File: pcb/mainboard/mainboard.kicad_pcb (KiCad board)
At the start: 10 copper layers, 165 x 121 mm, 608 parts, among them J1 CONN_PCIE_PWR_8PIN, J10 FAN_01, J11 XILINX_JTAG, J12 JUMPER_0402_SPDT, J13 JUMPER_0402_SPDT, J14 RJ45, J15 PMOD_HOST, J16 SMPM, J17 SMPM, J18 SMPM, J19 SMPM, J2 CONN_IBC_MGMT, J20 SMPM, J21 SMPM, J22 SMPM, J23 SMPM, J24 SMPM, J25 SMPM, J26 SMPM, J27 0826-1G1T-23-F, J28 SMPM, J29 SMPM, J3 CONN_01X03, J30 SMPM, J31 SMPM, J32 SMPM, J33 SMPM, J34 SMPM, J35 SMPM, J36 SMPM, J37 SMPM, J38 SMPM, J39 SMPM, J4 CONN_01X05, J40 SMPM, J41 SMPM, J42 SMPM, J43 SMPM, J44 SMPM, J45 SMPM, J46 SMPM, J47 SMPM, J48 CONN_01X10, J5 XILINX_JTAG, J6 CONN_SFP_HOST, J7 SFP_CAGE, J8 FAN_01, J9 CONN_01X03, K1 RELAY_TE_HF3_96, K2 RELAY_TE_HF3_96, K3 RELAY_TE_HF3_96, K4 RELAY_TE_HF3_96, M1 960-23-23-F-AB-0, SW1 SWITCH, SW2 SWITCH, U1 STM32L031C6U6, U10 MAX40026, U11 MAX40026, U12 MAX40026, U13 MAX40026, U14 MAX40026, U15 MAX40026, U16 MAX40026, U17 MAX40026, U18 MAX40026, U19 MAX40026, U2 MYMGK1R812ERSR, U20 MAX40026, U21 DAC60508, U22 DAC60508, U23 STM32H735-UFBGA176-25, U24 AT24MAC402, U25 ADM3101E_QFN, U26 LMR70503, U27 SIT9121AI-2BF-XXS200.000000G, U28 SIT9121AI-2BF-XXS156.250000G, U29 HMC675LP3E, U3 MYMGK00504ERSR, U30 SIT9121AI-2BF-XXS200.000000G, U31 ECS-1612MV-250-CN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

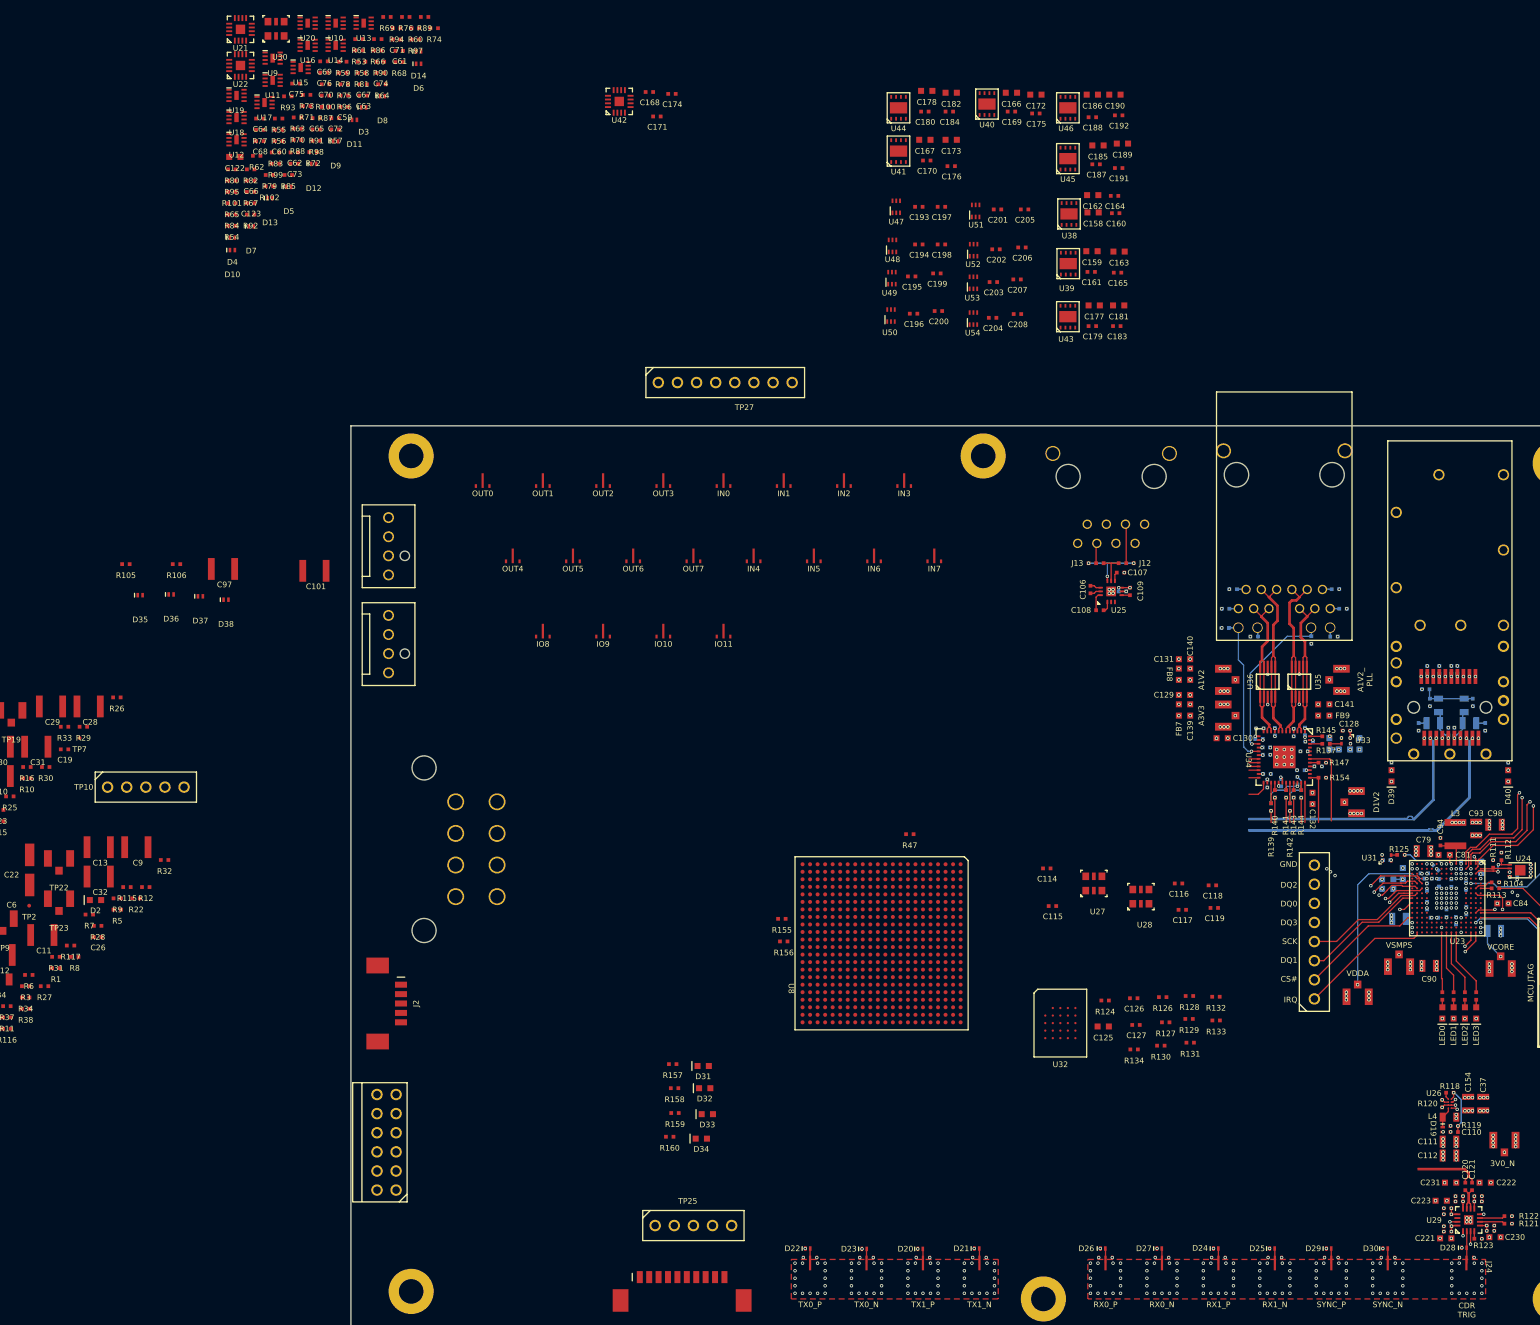
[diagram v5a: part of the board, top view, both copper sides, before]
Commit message: Started layout of rear panel IO connectors and associated drivers/comparators
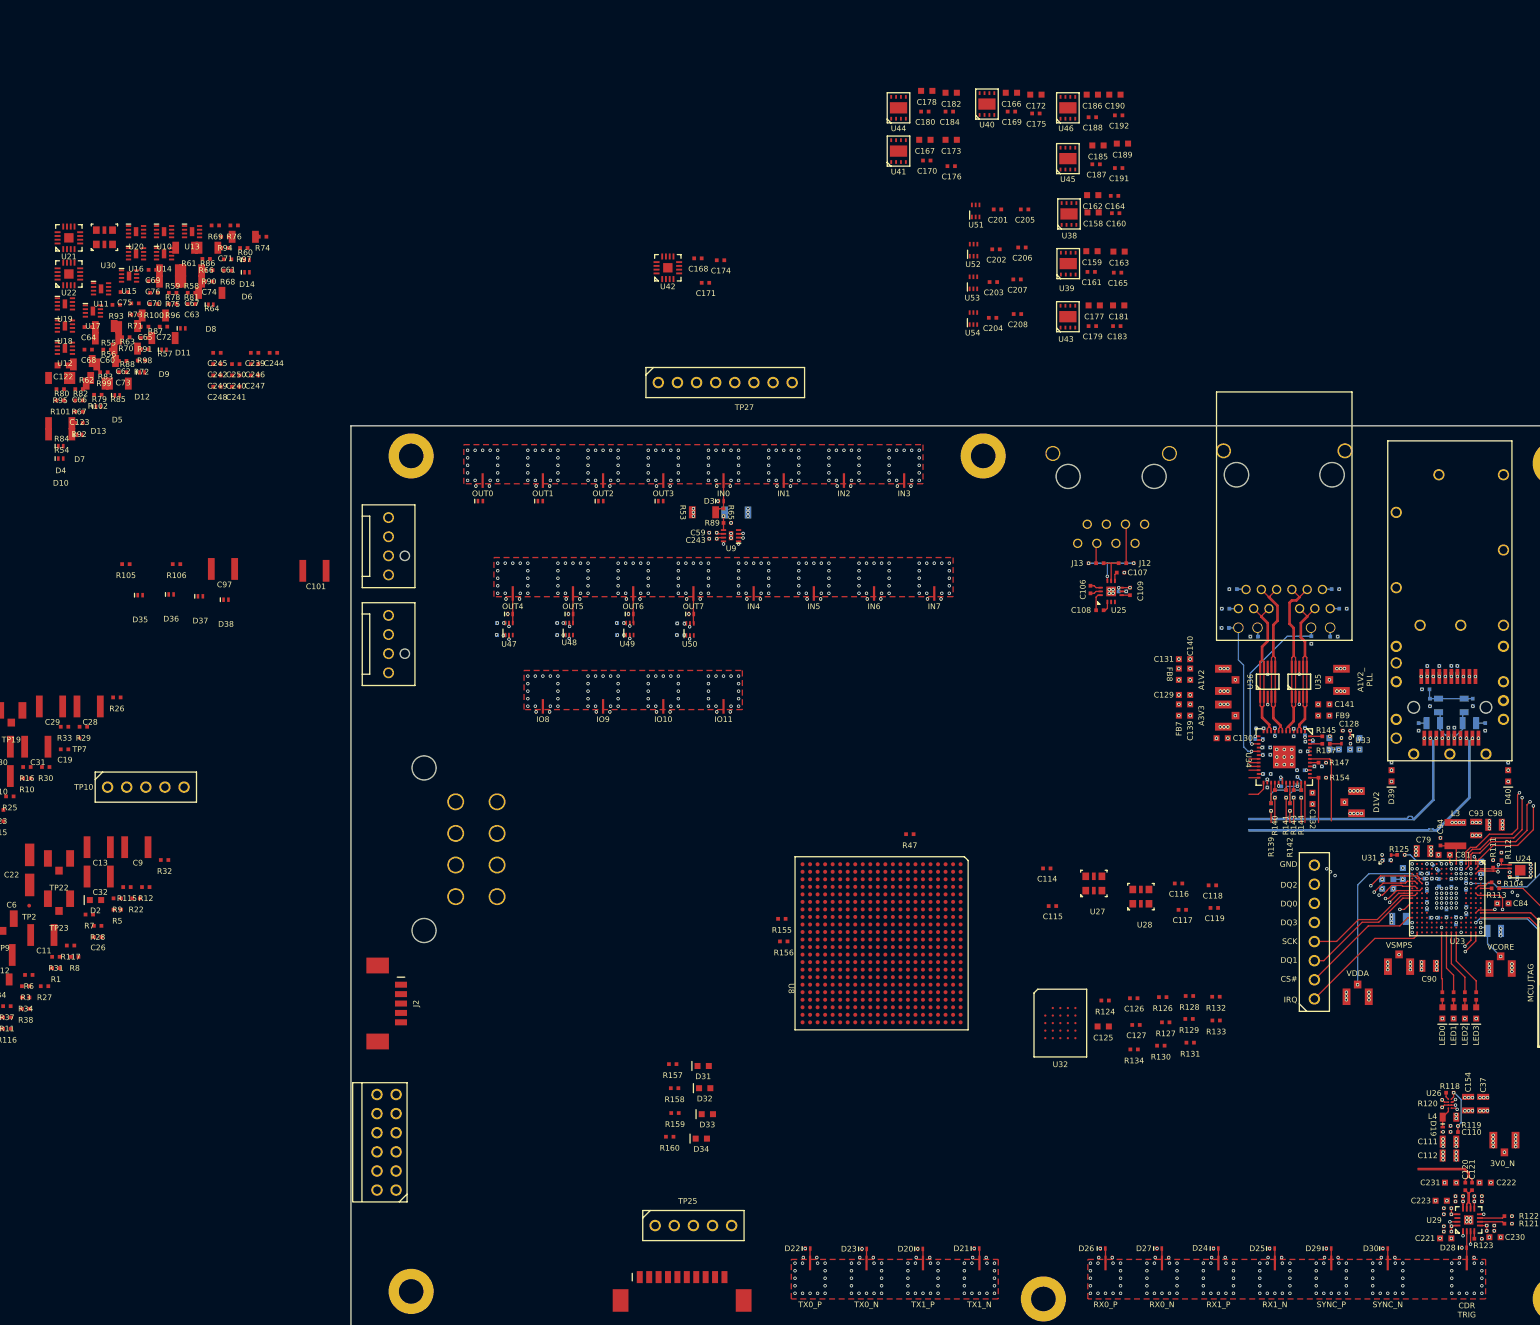
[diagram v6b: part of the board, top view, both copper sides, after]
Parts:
- added C239: 0.47 uF, azonenberg_pcb:EIA_0402_CAP_NOSILK, F.Cu at (102.2, 10.3)
- added C240: 0.47 uF, azonenberg_pcb:EIA_0402_CAP_NOSILK, F.Cu at (99.7, 13.3)
- added C241: 0.47 uF, azonenberg_pcb:EIA_0402_CAP_NOSILK, F.Cu at (99.7, 14.8)
- added C242: 0.47 uF, azonenberg_pcb:EIA_0402_CAP_NOSILK, F.Cu at (97.2, 11.8)
- added C243: 0.47 uF, azonenberg_pcb:EIA_0402_CAP_NOSILK, F.Cu at (163.1, 35.0)
- added C244: 0.47 uF, azonenberg_pcb:EIA_0402_CAP_NOSILK, F.Cu at (104.7, 10.3)
- added C245: 0.47 uF, azonenberg_pcb:EIA_0402_CAP_NOSILK, F.Cu at (97.2, 10.3)
- added C246: 0.47 uF, azonenberg_pcb:EIA_0402_CAP_NOSILK, F.Cu at (102.2, 11.8)
- added C247: 0.47 uF, azonenberg_pcb:EIA_0402_CAP_NOSILK, F.Cu at (102.2, 13.3)
- added C248: 0.47 uF, azonenberg_pcb:EIA_0402_CAP_NOSILK, F.Cu at (97.2, 14.8)
- added C249: 0.47 uF, azonenberg_pcb:EIA_0402_CAP_NOSILK, F.Cu at (97.2, 13.3)
- added C250: 0.47 uF, azonenberg_pcb:EIA_0402_CAP_NOSILK, F.Cu at (99.7, 11.8)
- added D41: SZESD7471N2T5G, azonenberg_pcb:SOD882, F.Cu at (132.2, 30.0)
- added D42: SZESD7471N2T5G, azonenberg_pcb:SOD882, F.Cu at (156.2, 30.0)
- added D43: SZESD7471N2T5G, azonenberg_pcb:SOD882, F.Cu at (152.2, 45.0)
- added D44: SZESD7471N2T5G, azonenberg_pcb:SOD882, F.Cu at (140.2, 30.0)
- added D45: SZESD7471N2T5G, azonenberg_pcb:SOD882, F.Cu at (136.2, 45.0)
- added D46: SZESD7471N2T5G, azonenberg_pcb:SOD882, F.Cu at (160.2, 45.0)
- added D47: SZESD7471N2T5G, azonenberg_pcb:SOD882, F.Cu at (148.2, 30.0)
- added D48: SZESD7471N2T5G, azonenberg_pcb:SOD882, F.Cu at (144.2, 45.0)
- C193, C194, C195, C196, C197, C198, C199, C200: moved to B.Cu
- R53, R54, R55, R56, R57, R58, R59, R60, R61, R62, R63, R64, R78, R79, R80, R81, R82, R83, R84, R85, R86, R87, R88: footprint azonenberg_pcb:EIA_0402_RES_NOSILK -> azonenberg_pcb:EIA_1206_CAP_NOSILK
- R77: footprint azonenberg_pcb:EIA_0402_RES_NOSILK -> azonenberg_pcb:EIA_1206_CAP_NOSILK; moved to B.Cu
- moved U9 87.9 mm to (165.5, 34.6), turned to 180 degrees
- moved C197 81.6 mm to (134.9, 47.8), turned to 180 degrees
- moved R77 81.2 mm to (166.2, 31.5), turned to 180 degrees
- moved C193 78.4 mm to (134.9, 46.2), turned to 180 degrees
- moved R89 78.3 mm to (165.0, 32.9)
- moved R65 77.2 mm to (164.5, 31.5), turned to -90 degrees
- moved R53 76.6 mm to (161.9, 31.5), turned to 180 degrees
- moved U47 76.1 mm to (136.0, 47.0)
- moved C59 74.8 mm to (163.1, 34.2), turned to 180 degrees
- moved C198 72.4 mm to (142.9, 47.8), turned to 180 degrees
- moved D3 70.7 mm to (164.2, 30.0)
- moved C194 69.2 mm to (142.9, 46.2), turned to 180 degrees
- moved U48 66.6 mm to (144.0, 47.0)
- moved C199 63.8 mm to (150.8, 47.8), turned to 180 degrees
- moved C195 60.1 mm to (150.8, 46.2), turned to 180 degrees
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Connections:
- J24 pad 1: (no net) -> /Transceivers/CDRTRIG_IN
- J24 pad 2: (no net) -> /GND
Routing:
- net /GND: track 754.8 -> 1074.5 mm, vias 426 -> 796
- net /3V3: track 290.5 -> 324.5 mm, vias 65 -> 75
- net /Connectors/IN0: track 0.00 -> 4.98 mm
- net /Connectors/OUT7: track 0.00 -> 4.00 mm
- net /Connectors/OUT6: track 0.00 -> 3.95 mm
- net /Connectors/OUT5: track 0.00 -> 3.93 mm
- net /Connectors/OUT4: track 0.00 -> 3.93 mm
- net /Inputs/VFE_IN0: track 0.00 -> 1.85 mm, vias 0 -> 1
- net /Inputs/TRIGIN_0_P: track 0.00 -> 0.35 mm, vias 0 -> 1
- net /Inputs/TRIGIN_0_N: track 0.00 -> 0.35 mm, vias 0 -> 1
- net /Output/VCCIO_5: track 0.00 -> 0.20 mm, vias 0 -> 1
- net /Output/VCCIO_6: track 0.00 -> 0.10 mm, vias 0 -> 1
- net /Output/VCCIO_4: track 0.00 -> 0.10 mm, vias 0 -> 1
- net /Output/VCCIO_7: track 0.00 -> 0.07 mm, vias 0 -> 1

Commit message: Grouped remaining components by subsystem, continued layout of IO area
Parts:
- C160, C164, R78, R79, R80: moved to B.Cu
- moved U3 224.9 mm to (236.8, 150.3)
- moved TP1 213.1 mm to (242.8, 146.8)
- moved TP19 212.1 mm to (261.5, 148.8)
- moved R29 209.3 mm to (268.8, 149.2)
- moved FB2 200.9 mm to (255.0, 147.0)
- moved C2 194.3 mm to (228.0, 147.0)
- moved C12 189.6 mm to (249.2, 147.2)
- moved C5 189.2 mm to (227.0, 152.8)
- moved R28 187.5 mm to (257.2, 151.5)
- moved R12 180.6 mm to (254.2, 151.2)
- moved R9 179.2 mm to (249.2, 152.0)
- moved C9 173.8 mm to (243.2, 151.0)
- moved R3 159.2 mm to (221.2, 149.2)
- moved R1 155.1 mm to (221.2, 146.0)
- moved R35 143.9 mm to (176.2, 153.5)
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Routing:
- net /GND: track 1074.5 -> 1158.0 mm, vias 796 -> 838
- net /VREF_SERDESIN: track 8.70 -> 69.6 mm, vias 1 -> 2
- net /Transceivers/FASTSYNC_TX_N: track 1.92 -> 60.3 mm, vias 0 -> 1
- net /Transceivers/CDRTRIG_RX_P: track 8.23 -> 61.7 mm, vias 0 -> 2
- net /Transceivers/CDRTRIG_RX_N: track 8.53 -> 61.7 mm, vias 0 -> 2
- net /3V3: track 324.5 -> 376.7 mm, vias 75 -> 81
- net /Transceivers/FASTSYNC_TX_P: track 1.93 -> 53.7 mm, vias 0 -> 1
- net /Transceivers/BERT_RX1_N: track 1.95 -> 47.1 mm, vias 0 -> 1
- net /Power Supply/3V0_N_EN: track 5.37 -> 47.4 mm, vias 1 -> 2
- net /Transceivers/BERT_RX1_P: track 1.95 -> 41.1 mm, vias 0 -> 1
- net /Transceivers/BERT_RX0_N: track 1.95 -> 35.5 mm, vias 0 -> 1
- net /Transceivers/BERT_RX0_P: track 1.95 -> 30.8 mm, vias 0 -> 1
- net /Output/VCCIO_4: track 0.10 -> 10.5 mm, vias 1 -> 4
- net /Connectors/IN3: track 0.00 -> 5.12 mm
- net /Connectors/IN1: track 0.00 -> 5.08 mm
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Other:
- board text added: "12V input"
- board text added: "1V0 supply"
- board text added: "1V2 supply"
- board text added: "1V8 supply"
- board text added: "3V3 supply"
- board text added: "5V0 supply"
- board text added: "GTX_1V0 supply"
- board text added: "GTX_1V8 supply"
- board text added: "Management"
- board text added: "Power switches"

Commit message: Initial FPGA routing
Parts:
- added R165: 4.7K, azonenberg_pcb:EIA_0402_RES_NOSILK, B.Cu at (253.0, 104.8)
- C125, C126, C127, C177, C181, C201, C203, C205, C207, C209, C210, C211, C212, R1, R101, R124, R126, R127, R128, R129, R3, R81, R82, R83, R84, R85, R87, U55, U56: moved to B.Cu
- C160, C164: moved to F.Cu
- moved C18 221.5 mm to (235.9, 149.3)
- moved C30 221.5 mm to (245.5, 149.5)
- moved C33 221.5 mm to (245.1, 155.9)
- moved R19 221.5 mm to (241.1, 148.9)
- moved R37 221.5 mm to (254.5, 155.5)
- moved TP7 221.5 mm to (240.5, 154.9)
- moved C24 221.5 mm to (235.7, 155.1)
- moved FB5 221.5 mm to (250.7, 153.5)
- moved R22 221.5 mm to (240.7, 151.7)
- moved R25 221.5 mm to (249.7, 148.7)
- moved R33 221.5 mm to (258.9, 155.9)
- moved TP23 221.5 mm to (255.7, 149.5)
- moved U7 221.5 mm to (226.0, 153.0)
- moved K3 143.8 mm to (156.5, 66.5), turned to 180 degrees
- moved TP28 142.9 mm to (130.0, 62.5), turned to 90 degrees
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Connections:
- D11 pad 2: /Connectors/IN8 -> /Connectors/IO8
- D12 pad 2: /Connectors/IN9 -> /Connectors/IO11
- D13 pad 2: /Connectors/IN10 -> /Connectors/IO9
- D14 pad 2: /Connectors/IN11 -> /Connectors/IO10
- U21 pad 10: /Inputs/VREF_IN6 -> /Inputs/VREF_IN1
- U21 pad 11: /Inputs/VREF_IN7 -> /Inputs/VREF_IN0
- U21 pad 2: /Inputs/VREF_IN0 -> /Inputs/VREF_IN3
- U21 pad 3: /Inputs/VREF_IN1 -> /Inputs/VREF_IN2
- U21 pad 4: /Inputs/VREF_IN2 -> /Inputs/VREF_IN7
- U21 pad 5: /Inputs/VREF_IN3 -> /Inputs/VREF_IN6
- U21 pad 8: /Inputs/VREF_IN4 -> /Inputs/VREF_IN5
- U21 pad 9: /Inputs/VREF_IN5 -> /Inputs/VREF_IN4
- U8 pad A10: unconnected-(U8-PadA10) -> /1000base-T PHY/RGMII_TX_EN
- U8 pad A11: unconnected-(U8-PadA11) -> /1000base-T PHY/ETH_RXD2
- U8 pad A13: /Output/OUT10_3V3 -> unconnected-(U8-PadA13)
- U8 pad A14: /Output/OUT11_3V3 -> unconnected-(U8-PadA14)
- U8 pad A16: /Connectors/OE11B -> unconnected-(U8-PadA16)
- U8 pad A8: unconnected-(U8-PadA8) -> /1000base-T PHY/RGMII_TXD1
- U8 pad A9: unconnected-(U8-PadA9) -> /1000base-T PHY/RGMII_TXD3
- U8 pad AA10: unconnected-(U8-PadAA10) -> /Inputs/TRIGIN_3_P
- U8 pad AA17: /1V8 -> /3V3
- U8 pad AA20: unconnected-(U8-PadAA20) -> /Connectors/OE10B
- U8 pad AA3: unconnected-(U8-PadAA3) -> /Connectors/OUT0
- U8 pad AA4: unconnected-(U8-PadAA4) -> /Connectors/OUT2
- U8 pad AA5: unconnected-(U8-PadAA5) -> /Inputs/TRIGIN_0_P
- U8 pad AA6: unconnected-(U8-PadAA6) -> /Inputs/TRIGIN_2_P
- U8 pad AA8: unconnected-(U8-PadAA8) -> /Inputs/TRIGIN_4_N
- U8 pad AA9: unconnected-(U8-PadAA9) -> /Inputs/TRIGIN_4_P
- U8 pad AB10: unconnected-(U8-PadAB10) -> /Inputs/TRIGIN_3_N
- U8 pad AB14: /1V8 -> /3V3
- U8 pad AB2: unconnected-(U8-PadAB2) -> /Connectors/OUT1
- U8 pad AB21: unconnected-(U8-PadAB21) -> /Connectors/OE11B
- U8 pad AB3: unconnected-(U8-PadAB3) -> /Connectors/OUT3
- U8 pad AB5: unconnected-(U8-PadAB5) -> /Inputs/TRIGIN_0_N
- U8 pad AB6: unconnected-(U8-PadAB6) -> /Inputs/TRIGIN_2_N
- U8 pad AB7: unconnected-(U8-PadAB7) -> /Inputs/TRIGIN_1_N
- U8 pad AB8: unconnected-(U8-PadAB8) -> /Inputs/TRIGIN_1_P
- U8 pad B10: unconnected-(U8-PadB10) -> /1000base-T PHY/RGMII_TX_CLK
- U8 pad B11: unconnected-(U8-PadB11) -> /1000base-T PHY/ETH_RXD3
- U8 pad B12: /Output/OUT7_3V3 -> unconnected-(U8-PadB12)
- U8 pad B13: /Connectors/OE9A -> unconnected-(U8-PadB13)
- U8 pad B16: /Connectors/OE10B -> unconnected-(U8-PadB16)
- U8 pad B8: unconnected-(U8-PadB8) -> /1000base-T PHY/RGMII_TXD0
- U8 pad C10: /1000base-T PHY/RGMII_TXD3 -> unconnected-(U8-PadC10)
- U8 pad C12: /Output/OUT6_3V3 -> unconnected-(U8-PadC12)
- U8 pad C13: /Connectors/OE8A -> unconnected-(U8-PadC13)
- U8 pad C14: /Connectors/OE8B -> unconnected-(U8-PadC14)
- U8 pad C15: /Connectors/OE9B -> unconnected-(U8-PadC15)
- U8 pad C9: unconnected-(U8-PadC9) -> /1000base-T PHY/RGMII_TXD2
- U8 pad D10: /1000base-T PHY/RGMII_TX_CLK -> unconnected-(U8-PadD10)
- U8 pad D11: /1000base-T PHY/ETH_MDC -> /1000base-T PHY/ETH_RXD1
- U8 pad D14: /Connectors/OE11A -> unconnected-(U8-PadD14)
- U8 pad E14: /Connectors/OE10A -> unconnected-(U8-PadE14)
- U8 pad E9: /1000base-T PHY/ETH_RXD3 -> unconnected-(U8-PadE9)
- U8 pad F1: /Transceivers/SFP_TX_N -> /Transceivers/SFP_TX_P
- U8 pad F13: /1000base-T PHY/RGMII_TXD1 -> unconnected-(U8-PadF13)
- U8 pad F14: /1000base-T PHY/RGMII_TX_EN -> unconnected-(U8-PadF14)
- U8 pad F15: /Output/OUT8_3V3 -> unconnected-(U8-PadF15)
- U8 pad F16: /Output/OUT9_3V3 -> unconnected-(U8-PadF16)
- U8 pad F2: /Transceivers/SFP_TX_P -> /Transceivers/SFP_TX_N
- U8 pad F9: /1000base-T PHY/ETH_RXD2 -> unconnected-(U8-PadF9)
- U8 pad G12: /1000base-T PHY/ETH_RXD1 -> /1000base-T PHY/ETH_MDC
- U8 pad G13: /1000base-T PHY/RGMII_TXD2 -> unconnected-(U8-PadG13)
- U8 pad G15: /Output/OUT4_3V3 -> unconnected-(U8-PadG15)
- U8 pad G16: /Output/OUT5_3V3 -> unconnected-(U8-PadG16)
- U8 pad H14: /1000base-T PHY/RGMII_TXD0 -> unconnected-(U8-PadH14)
- U8 pad K1: /Inputs/TRIGIN_1_P -> unconnected-(U8-PadK1)
- U8 pad K2: /Inputs/TRIGIN_3_N -> unconnected-(U8-PadK2)
- U8 pad K3: /Inputs/TRIGIN_3_P -> unconnected-(U8-PadK3)
- U8 pad K4: Net-(R101-Pad2) -> Net-(R155-Pad2)
- U8 pad L1: /Inputs/TRIGIN_1_N -> unconnected-(U8-PadL1)
- U8 pad L3: /Inputs/TRIGIN_0_P -> unconnected-(U8-PadL3)
- U8 pad L4: /Inputs/TRIGIN_5_N -> unconnected-(U8-PadL4)
- U8 pad L5: /Inputs/TRIGIN_5_P -> unconnected-(U8-PadL5)
- U8 pad M1: /Inputs/TRIGIN_2_N -> unconnected-(U8-PadM1)
- U8 pad M2: /Inputs/TRIGIN_2_P -> unconnected-(U8-PadM2)
- U8 pad M3: /Inputs/TRIGIN_0_N -> unconnected-(U8-PadM3)
- U8 pad M5: /Inputs/TRIGIN_8_P -> unconnected-(U8-PadM5)
- U8 pad N2: /Inputs/TRIGIN_4_N -> unconnected-(U8-PadN2)
- U8 pad N3: /Inputs/TRIGIN_4_P -> unconnected-(U8-PadN3)
- U8 pad N4: /Inputs/TRIGIN_8_N -> unconnected-(U8-PadN4)
- U8 pad P1: /Inputs/TRIGIN_7_P -> unconnected-(U8-PadP1)
- U8 pad P2: /Inputs/TRIGIN_6_P -> unconnected-(U8-PadP2)
- U8 pad R1: /Inputs/TRIGIN_7_N -> unconnected-(U8-PadR1)
- U8 pad R2: /Inputs/TRIGIN_6_N -> unconnected-(U8-PadR2)
- U8 pad R3: /Inputs/CLK_200_P -> unconnected-(U8-PadR3)
- U8 pad R6: unconnected-(U8-PadR6) -> /Inputs/TRIGIN_7_N
- U8 pad R7: unconnected-(U8-PadR7) -> /Inputs/TRIGIN_7_P
- U8 pad T1: /Inputs/TRIGIN_9_P -> unconnected-(U8-PadT1)
- U8 pad T10: unconnected-(U8-PadT10) -> /Inputs/TRIGIN_11_N
- U8 pad T11: unconnected-(U8-PadT11) -> /Inputs/TRIGIN_11_P
- U8 pad T13: /Connectors/OUT2 -> unconnected-(U8-PadT13)
- U8 pad T14: Net-(R156-Pad2) -> Net-(R102-Pad2)
- U8 pad T18: unconnected-(U8-PadT18) -> /Output/OUT8_3V3
- U8 pad T20: unconnected-(U8-PadT20) -> /Connectors/OE10A
- U8 pad T21: unconnected-(U8-PadT21) -> /Output/OUT4_3V3
- U8 pad T22: /1V8 -> /3V3
- U8 pad T3: /Inputs/CLK_200_N -> unconnected-(U8-PadT3)
- U8 pad T5: /Inputs/TRIGIN_11_P -> unconnected-(U8-PadT5)
- U8 pad T6: Net-(R155-Pad2) -> Net-(R101-Pad2)
- U8 pad U1: /Inputs/TRIGIN_9_N -> unconnected-(U8-PadU1)
- U8 pad U13: /Connectors/OUT3 -> unconnected-(U8-PadU13)
- U8 pad U17: unconnected-(U8-PadU17) -> /Connectors/OE8A
- U8 pad U18: unconnected-(U8-PadU18) -> /Output/OUT9_3V3
- U8 pad U19: /1V8 -> /3V3
- U8 pad U2: /Inputs/TRIGIN_10_P -> unconnected-(U8-PadU2)
- U8 pad U20: unconnected-(U8-PadU20) -> /Connectors/OE11A
- U8 pad U21: unconnected-(U8-PadU21) -> /Output/OUT5_3V3
- U8 pad U22: unconnected-(U8-PadU22) -> /Output/OUT6_3V3
- U8 pad U5: /Inputs/TRIGIN_11_N -> unconnected-(U8-PadU5)
- U8 pad U6: unconnected-(U8-PadU6) -> /Inputs/TRIGIN_9_N
- U8 pad U7: unconnected-(U8-PadU7) -> /Inputs/TRIGIN_9_P
- U8 pad U8: unconnected-(U8-PadU8) -> /Inputs/TRIGIN_8_P
- U8 pad V10: unconnected-(U8-PadV10) -> /Inputs/TRIGIN_10_P
- U8 pad V12: /Connectors/OUT1 -> unconnected-(U8-PadV12)
- U8 pad V13: /Connectors/OUT0 -> unconnected-(U8-PadV13)
- U8 pad V16: /1V8 -> /3V3
- U8 pad V18: unconnected-(U8-PadV18) -> /Connectors/OE9A
- U8 pad V2: /Inputs/TRIGIN_10_N -> unconnected-(U8-PadV2)
- U8 pad V22: unconnected-(U8-PadV22) -> /Output/OUT7_3V3
- U8 pad V5: Net-(R102-Pad2) -> Net-(R156-Pad2)
- U8 pad V8: unconnected-(U8-PadV8) -> /Inputs/TRIGIN_8_N
- U8 pad W10: unconnected-(U8-PadW10) -> /Inputs/TRIGIN_10_N
- U8 pad W11: unconnected-(U8-PadW11) -> /Inputs/TRIGIN_5_P
- U8 pad W21: unconnected-(U8-PadW21) -> /Output/OUT10_3V3
- U8 pad W22: unconnected-(U8-PadW22) -> /Output/OUT11_3V3
- U8 pad W6: unconnected-(U8-PadW6) -> /Inputs/TRIGIN_6_P
- U8 pad Y11: unconnected-(U8-PadY11) -> /Inputs/TRIGIN_5_N
- U8 pad Y20: /1V8 -> /3V3
- U8 pad Y21: unconnected-(U8-PadY21) -> /Connectors/OE8B
- U8 pad Y22: unconnected-(U8-PadY22) -> /Connectors/OE9B
- U8 pad Y6: unconnected-(U8-PadY6) -> /Inputs/TRIGIN_6_N
- U8 pad Y7: unconnected-(U8-PadY7) -> /Inputs/CLK_200_N
- U8 pad Y8: unconnected-(U8-PadY8) -> /Inputs/CLK_200_P
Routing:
- net /GND: track 1158.0 -> 1866.9 mm, vias 838 -> 1149
- net /3V3: track 376.7 -> 702.7 mm, vias 81 -> 135
- net /12V0: track 0.00 -> 164.7 mm, vias 0 -> 26
- net /Management/RX_DAC0_CS_N: track 18.9 -> 118.0 mm, vias 1 -> 4
- net /DAC_MISO: track 15.2 -> 110.7 mm, vias 1 -> 4
- net /DAC_SCK: track 17.0 -> 110.7 mm, vias 1 -> 4
- net /5V0: track 1.59 -> 89.9 mm, vias 2 -> 10
- net /TX_DAC_CS_N: track 14.9 -> 99.0 mm, vias 1 -> 3
- net /Management/FAN1_TACH: track 0.00 -> 78.3 mm
- net /Management/FAN1_PWM: track 33.4 -> 110.7 mm
- net /Management/RX_DAC1_CS_N: track 18.0 -> 90.3 mm, vias 1 -> 3
- net /1V2: track 136.4 -> 202.5 mm, vias 11 -> 22
- net /Transceivers/FASTSYNC_TX_N: track 60.3 -> 2.47 mm, vias 1 -> 2
- net /1V8: track 0.00 -> 54.2 mm, vias 0 -> 21
- net /Transceivers/FASTSYNC_TX_P: track 53.7 -> 2.49 mm, vias 1 -> 2
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- added copper zone on F.Cu, net /12V0
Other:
- board text added: "12V IN"
- board text added: "12V0"
- board text added: "1V2"
- board text added: "3V3"
- board text added: "DAC_MISO"
- board text added: "DAC_MOSI"
- board text added: "DAC_SCK"
- board text added: "FAN1"
- board text added: "FAN2"
- board text added: "IBC MGMT"
- board text added: "PMOD"
- board text added: "RX0_CS_N"
- board text added: "RX1_CS_N"
- board text added: "TX_CS_N"
- board text removed: "1V2 supply"
- board text removed: "FPGA flash"
- board text removed: "Output level"
